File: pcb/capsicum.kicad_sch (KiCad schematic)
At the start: 69 parts, among them J2 Screw_Terminal_01x02, J3 USB-C 16+8 USB 2.0, Q1 NS2101P, Q2 BC817-16LT3G, SW1 SW_SPDT, SW3 SW_SPDT, U1 ESP32-C3-WROOM-02, U2 TQ33E-1, U3 AP2112K, U4 MCP73831

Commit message: feat: associate MPN and BOM details for Schottky diode
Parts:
- D2: footprint Resistor_SMD:R_0603_1608Metric -> Diode_SMD:D_SOD-123F; Link (none) -> https://www.pcbway.com/components/detail/PMEG3020EH115/9231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; MANUFACTURER (none) -> Nexperia USA Inc.; MPN (none) -> PMEG3020EH,115; Package (none) -> SOD-123F; Vendor (none) -> PCBWay
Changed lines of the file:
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@@
       (effects (font (size 1.27 1.27)))
     )
-    (property "Footprint" "Resistor_SMD:R_0603_1608Metric" (at 105.41 62.23 0)
+    (property "Footprint" "Diode_SMD:D_SOD-123F" (at 105.41 62.23 0)
       (effects (font (size 1.27 1.27)) hide)
     )
-    (property "Datasheet" "~" (at 105.41 62.23 0)
+    (property "Datasheet" "https://assets.nexperia.com/documents/data-sheet/PMEG3020EH.pdf" (at 105.41 62.23 0)
       (effects (font (size 1.27 1.27)) hide)
     )
-    (property "MPN" "" (at 105.41 62.23 0)
+    (property "MPN" "PMEG3020EH,115" (at 105.41 62.23 0)
       (effects (font (size 1.27 1.27)) hide)
     )
-    (property "Package" "" (at 105.41 62.23 0)
+    (property "Package" "SOD-123F" (at 105.41 62.23 0)
       (effects (font (size 1.27 1.27)) hide)
     )
+    (property "Link" "https://www.pcbway.com/components/detail/PMEG3020EH115/92316/" (at 105.41 62.23 0)
+      (effects (font (size 1.27 1.27)) hide)
+    )
+    (property "MANUFACTURER" "Nexperia USA Inc." (at 105.41 62.23 0)
+      (effects (font (size 1.27 1.27)) hide)
+    )
+    (property "Vendor" "PCBWay" (at 105.41 62.23 0)
+      (effects (font (size 1.27 1.27)) hide)
+    )

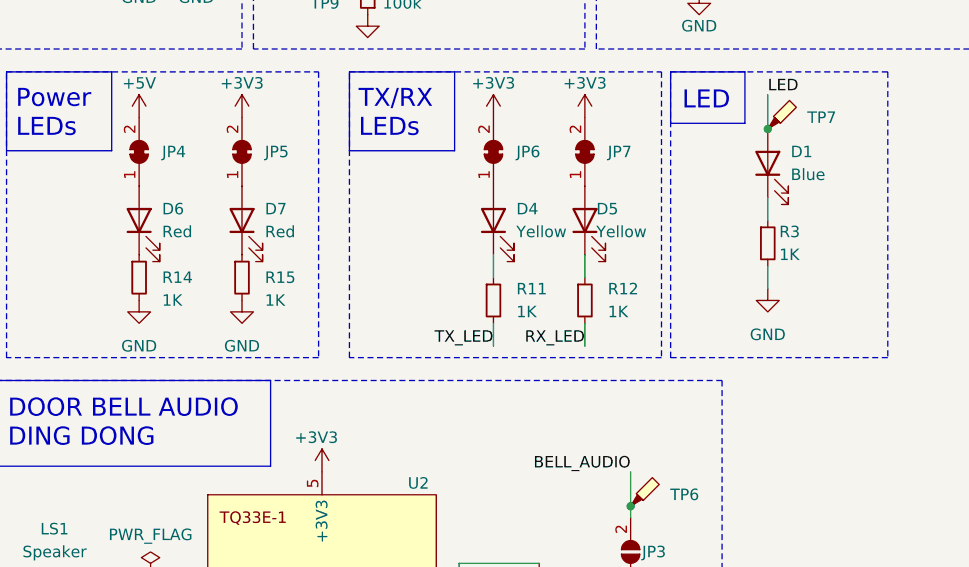
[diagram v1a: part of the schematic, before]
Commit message: feat: associate MPN and BOM details for some resistor values
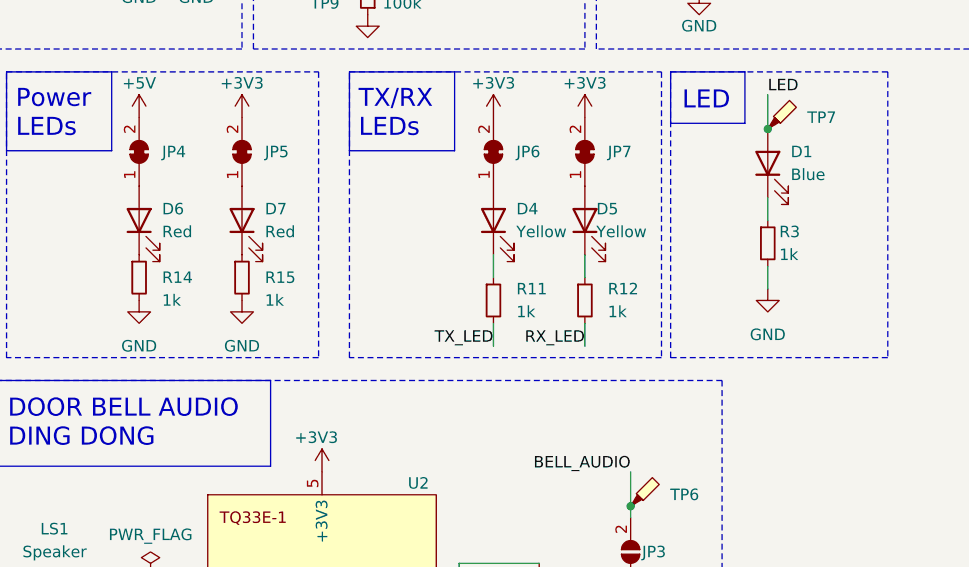
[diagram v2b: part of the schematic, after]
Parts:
- C1, C2, C3, C4, C5, C6, C7, C8: Package (none) -> 0603
- C9: Link (none) -> https://www.pcbway.com/components/detail/06033C104KAT4A/927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; MPN (none) -> 06033C104KAT4A; Package (none) -> 0603; Vendor (none) -> PCBWay
- R1, R13, R7, R8, R9: Link (none) -> https://www.pcbway.com/components/detail/RC0603FR0710KL/462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; MANUFACTURER (none) -> YAGEO; MPN (none) -> RC0603FR-0710KL; Package (none) -> 0603; Vendor (none) -> PCBWay
- R11, R12, R14, R15, R3: value 1K -> 1k; Link (none) -> https://www.pcbway.com/components/detail/RC0603FR071KL/4622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; MANUFACTURER (none) -> Yageo; MPN (none) -> RC0603FR-071KL; Package (none) -> 0603; Vendor (none) -> PCBWay
- R2, R5: Link (none) -> https://www.pcbway.com/components/detail/ERJ3GEYJ512V/42789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; MANUFACTURER (none) -> Panasonic; MPN (none) -> ERJ-3GEYJ512V; Package (none) -> 0603; Vendor (none) -> PCBWay
- R4: Link (none) -> https://www.pcbway.com/components/detail/RC0603FR071KL/4622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; MANUFACTURER (none) -> Yageo; MPN (none) -> RC0603FR-071KL; Package (none) -> 0603; Vendor (none) -> PCBWay
- U1: MPN (none) -> ESP32-C3-WROOM-02; Package (none) -> SMD
- U2: MPN (none) -> TQ33E-1

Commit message: feat: associate MPN and BOM details for all resistors
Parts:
- R10, R6: Link (none) -> https://www.pcbway.com/components/detail/RMCF0603FT100K/512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; MANUFACTURER (none) -> Stackpole; MPN (none) -> RMCF0603FT100K; Package (none) -> 0603; Vendor (none) -> PCBWay
- R16: Link (none) -> https://www.pcbway.com/components/detail/RC0603FR071ML/2858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; MANUFACTURER (none) -> YAGEO; MPN (none) -> RC0603FR-071ML; Package (none) -> 0603; Vendor (none) -> PCBWay
- R17, R18: Link (none) -> https://www.pcbway.com/components/detail/RC0603JR0733RL/285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; MANUFACTURER (none) -> YAGEO; MPN (none) -> RC0603JR-0733RL; Package (none) -> 0603; Vendor (none) -> PCBWay
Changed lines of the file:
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@@
       (effects (font (size 1.27 1.27)) hide)
     )
-    (property "Datasheet" "~" (at 120.65 64.77 0)
-      (effects (font (size 1.27 1.27)) hide)
-    )
-    (property "MPN" "" (at 120.65 64.77 0)
-      (effects (font (size 1.27 1.27)) hide)
-    )
-    (property "Package" "" (at 120.65 64.77 0)
+    (property "Datasheet" "https://www.seielect.com/Catalog/SEI-RMCF_RMCP.pdf" (at 120.65 64.77 0)
+      (effects (font (size 1.27 1.27)) hide)
+    )
+    (property "MPN" "RMCF0603FT100K" (at 120.65 64.77 0)
+      (effects (font (size 1.27 1.27)) hide)
+    )
+    (property "Package" "0603" (at 120.65 64.77 0)
+      (effects (font (size 1.27 1.27)) hide)
+    )
+    (property "Link" "https://www.pcbway.com/components/detail/RMCF0603FT100K/512606/" (at 120.65 64.77 0)
+      (effects (font (size 1.27 1.27)) hide)
+    )
+    (property "MANUFACTURER" "Stackpole" (at 120.65 64.77 0)
+      (effects (font (size 1.27 1.27)) hide)
+    )
+    (property "Vendor" "PCBWay" (at 120.65 64.77 0)
       (effects (font (size 1.27 1.27)) hide)
     )
@@
       (effects (font (size 1.27 1.27)) hide)
     )
-    (property "Datasheet" "~" (at 217.17 22.86 0)
-      (effects (font (size 1.27 1.27)) hide)
-    )
-    (property "MPN" "" (at 217.17 22.86 0)
-      (effects (font (size 1.27 1.27)) hide)
-    )
-    (property "Package" "" (at 217.17 22.86 0)
+    (property "Datasheet" "https://www.yageo.com/upload/media/product/productsearch/datasheet/rchip/PYu-RC_Group_51_RoHS_L_12.pdf" (at 217.17 22.86 0)
+      (effects (font (size 1.27 1.27)) hide)
+    )
+    (property "MPN" "RC0603FR-071ML" (at 217.17 22.86 0)
+      (effects (font (size 1.27 1.27)) hide)
+    )
+    (property "Package" "0603" (at 217.17 22.86 0)
+      (effects (font (size 1.27 1.27)) hide)
+    )
+    (property "Link" "https://www.pcbway.com/components/detail/RC0603FR071ML/285807/" (at 217.17 22.86 0)
+      (effects (font (size 1.27 1.27)) hide)
+    )
+    (property "MANUFACTURER" "YAGEO" (at 217.17 22.86 0)
+      (effects (font (size 1.27 1.27)) hide)
+    )
+    (property "Vendor" "PCBWay" (at 217.17 22.86 0)
       (effects (font (size 1.27 1.27)) hide)
     )
@@
       (effects (font (size 1.27 1.27)) hide)
     )
-    (property "Datasheet" "~" (at 29.21 46.99 0)
+    (property "Datasheet" "https://www.yageo.com/upload/media/product/productsearch/datasheet/rchip/PYu-RC_Group_51_RoHS_L_12.pdf" (at 29.21 46.99 0)
+      (effects (font (size 1.27 1.27)) hide)
+    )
+    (property "Link" "https://www.pcbway.com/components/detail/RC0603JR0733RL/285734/" (at 29.21 46.99 0)
+      (effects (font (size 1.27 1.27)) hide)
+    )
+    (property "MANUFACTURER" "YAGEO" (at 29.21 46.99 0)
+      (effects (font (size 1.27 1.27)) hide)
+    )
+    (property "MPN" "RC0603JR-0733RL" (at 29.21 46.99 0)
+      (effects (font (size 1.27 1.27)) hide)
+    )
+    (property "Package" "0603" (at 29.21 46.99 0)
+      (effects (font (size 1.27 1.27)) hide)
+    )
+    (property "Vendor" "PCBWay" (at 29.21 46.99 0)
       (effects (font (size 1.27 1.27)) hide)
     )
@@
       (effects (font (size 1.27 1.27)) hide)
     )
-    (property "Datasheet" "~" (at 29.21 44.45 0)
+    (property "Datasheet" "https://www.yageo.com/upload/media/product/productsearch/datasheet/rchip/PYu-RC_Group_51_RoHS_L_12.pdf" (at 29.21 44.45 0)
+      (effects (font (size 1.27 1.27)) hide)
+    )
+    (property "Link" "https://www.pcbway.com/components/detail/RC0603JR0733RL/285734/" (at 29.21 44.45 0)
+      (effects (font (size 1.27 1.27)) hide)
+    )
+    (property "MANUFACTURER" "YAGEO" (at 29.21 44.45 0)
+      (effects (font (size 1.27 1.27)) hide)
+    )
+    (property "MPN" "RC0603JR-0733RL" (at 29.21 44.45 0)
+      (effects (font (size 1.27 1.27)) hide)
+    )
+    (property "Package" "0603" (at 29.21 44.45 0)
+      (effects (font (size 1.27 1.27)) hide)
+    )
+    (property "Vendor" "PCBWay" (at 29.21 44.45 0)
       (effects (font (size 1.27 1.27)) hide)
     )
@@
       (effects (font (size 1.27 1.27)) hide)
     )
-    (property "Datasheet" "~" (at 212.09 43.18 0)
-      (effects (font (size 1.27 1.27)) hide)
-    )
-    (property "MPN" "" (at 212.09 43.18 0)
-      (effects (font (size 1.27 1.27)) hide)
-    )
-    (property "Package" "" (at 212.09 43.18 0)
-      (effects (font (size 1.27 1.27)) hide)
-    )
+    (property "Datasheet" "https://www.seielect.com/Catalog/SEI-RMCF_RMCP.pdf" (at 212.09 43.18 0)
+      (effects (font (size 1.27 1.27)) hide)
+    )
+    (property "MPN" "RMCF0603FT100K" (at 212.09 43.18 0)
+      (effects (font (size 1.27 1.27)) hide)
+    )
+    (property "Package" "0603" (at 212.09 43.18 0)
+      (effects (font (size 1.27 1.27)) hide)
+    )
+    (property "Link" "https://www.pcbway.com/components/detail/RMCF0603FT100K/512606/" (at 212.09 43.18 0)
+      (effects (font (size 1.27 1.27)) hide)
+    )
+    (property "MANUFACTURER" "Stackpole" (at 212.09 43.18 0)
+      (effects (font (size 1.27 1.27)) hide)
+    )
+    (property "Vendor" "PCBWay" (at 212.09 43.18 0)
+      (effects (font (size 1.27 1.27)) hide)
+    )

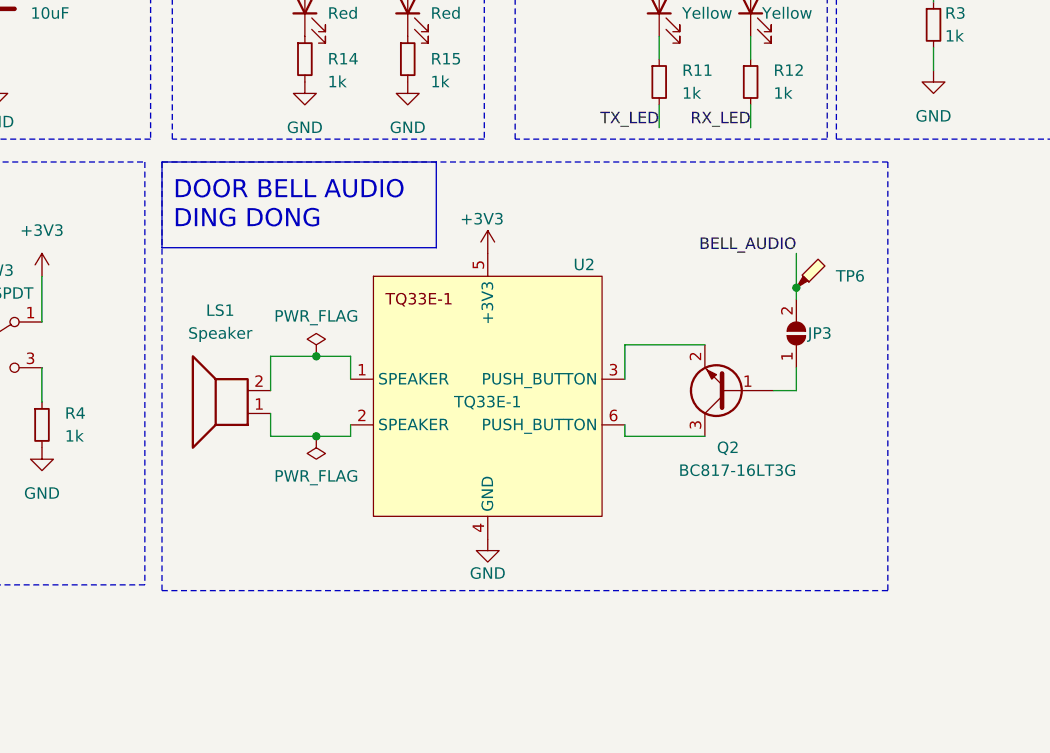
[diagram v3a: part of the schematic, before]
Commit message: refactor: udpate bell ding dong chip to integrate the speaker
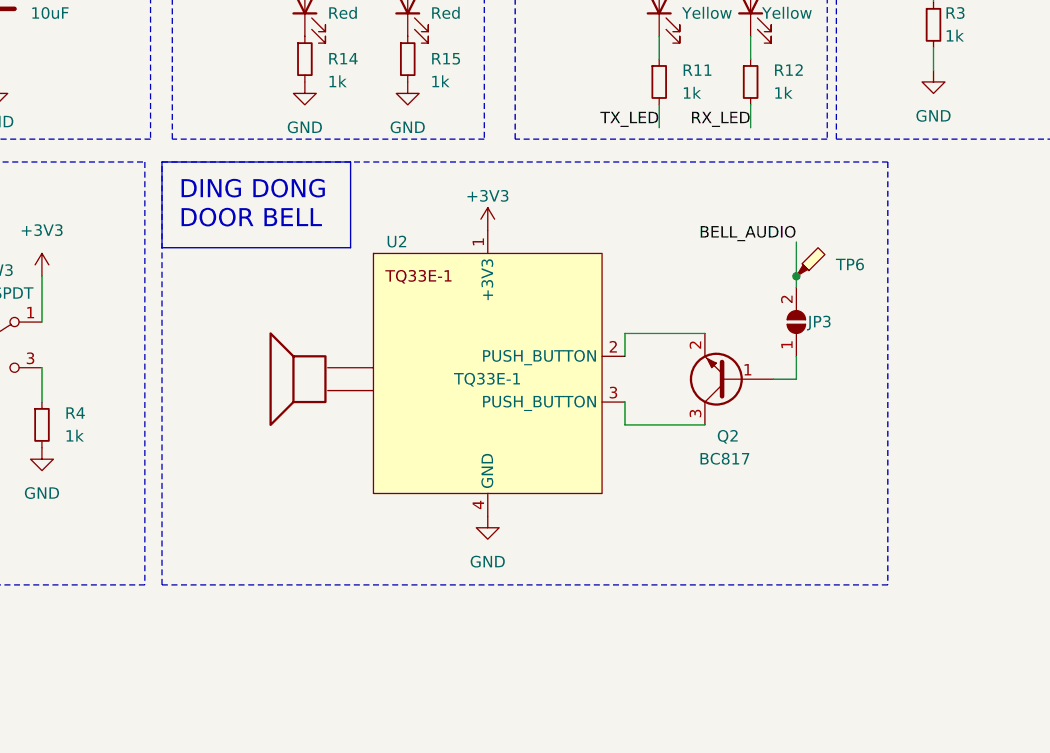
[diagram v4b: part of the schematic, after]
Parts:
- removed LS1: Speaker, Jumper:SolderJumper-2_P1.3mm_Open_RoundedPad1.0x1.5mm, symbol Device:Speaker
- removed U2: TQ33E-1, symbol bell_tq33e-1:TQ33E-1
- added U2: TQ33E-1, Connector_PinHeader_2.54mm:PinHeader_1x04_P2.54mm_Vertical, symbol Bell Dong Dong:TQ33E-1
- Q2: value BC817-16LT3G -> BC817
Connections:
- net +3V3: now also U2.1 (+3V3)
- net GND: now also U2.4 (GND)
- net at Q2.2 (E): now also U2.2 (PUSH_BUTTON)
- net at Q2.3 (C): now also U2.3 (PUSH_BUTTON)
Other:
- note added: "DING DONG DOOR BELL"
- note removed: "DOOR BELL AUDIO DING DONG"
- moved on the sheet: JP3, Q2, TP6

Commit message: feat: associate footprint for 16230 battery
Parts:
- BT1: footprint (none) -> Battery Holder CR123A:CR123_holder
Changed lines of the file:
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@@
       (effects (font (size 1.27 1.27)) (justify left))
     )
-    (property "Footprint" "" (at 101.6 36.576 90)
+    (property "Footprint" "Battery Holder CR123A:CR123_holder" (at 101.6 36.576 90)
       (effects (font (size 1.27 1.27)) hide)
     )
